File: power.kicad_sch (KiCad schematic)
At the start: 11 parts, among them U3 TLV71333PDQN

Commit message: schematic: more improvements towards R3
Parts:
- C14, C16: value 0.1uF -> 0u1
- R6: value 1.5K -> 1K5
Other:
- company: (none) -> Kalyan S, Vincent W, Kai G

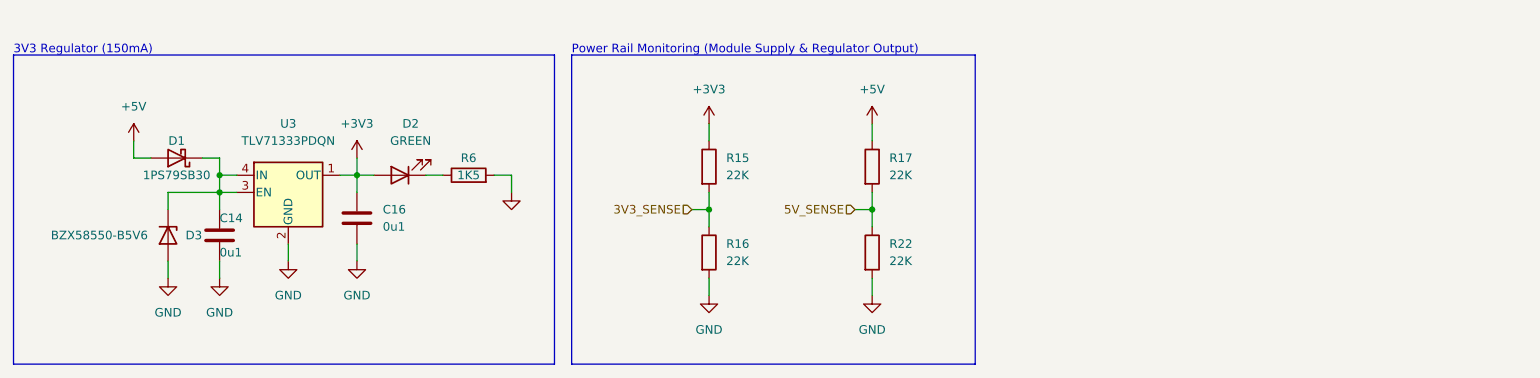
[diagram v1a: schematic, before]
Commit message: schematic: refresh sensors, mcu and redo pinout
    * update rp2040 -> rp2350b
    * update icm-42688p -> icm-45686
    * update bmm150 -> bmm350
    * add current sensing logic
    * change pinout count and update pinout
    * drop led and heater support
    * add can termination
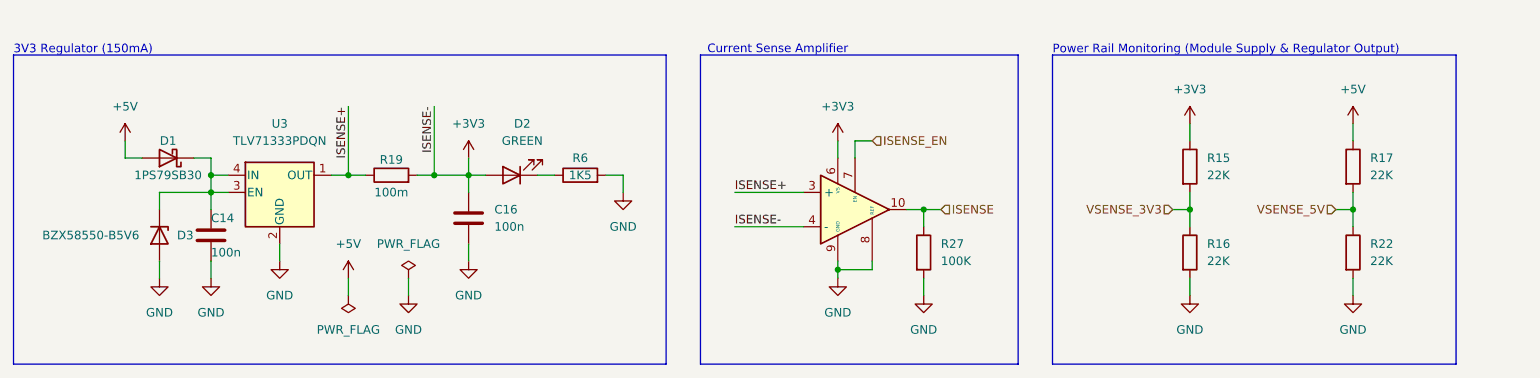
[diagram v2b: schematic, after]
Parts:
- added R19: 100m, symbol Device:R
- added R27: 100K, symbol Device:R
- added U9: ~, symbol Amplifier_Current_Extra:INA190
- C14, C16: value 0u1 -> 100n
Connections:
- net +3V3: now also R19.2, U9.4 (NC), U9.6 (VS); no longer U3.1 (OUT)
- net GND: now also R27.2, U9.8 (REF), U9.9 (GND)
- net 3V3_SENSE renamed VSENSE_3V3
- net 5V_SENSE renamed VSENSE_5V
- new net ISENSE: R27.1, U9.10
- new net ISENSE+: R19.1, U3.1 (OUT), U9.3 (+)
- new net ISENSE_EN: U9.7 (EN)
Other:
- note added: "Current Sense Amplifier"
- moved on the sheet: C14, C16, D1, D2, D3, R15, R16, R17, R22, R6, U3

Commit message: schematic: cleanup
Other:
- moved on the sheet: C14, C16, D1, D2, D3, R15, R16, R17, R19, R22, R27, R6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

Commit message: schematic: footprint assignment
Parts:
- R19: footprint (none) -> Resistor_SMD:R_0603_1608Metric
- R27: footprint (none) -> Resistor_SMD:R_0201_0603Metric
- U9: footprint (none) -> Package_DFN_QFN:Texas_RSW0010A_UQFN-10_1.4x1.8mm_P0.4mm
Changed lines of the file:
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@@
 			)
 		)
-		(property "Footprint" ""
+		(property "Footprint" "Package_DFN_QFN:Texas_RSW0010A_UQFN-10_1.4x1.8mm_P0.4mm"
 			(at 139.7 43.18 0)
 			(effects
@@
 		(pin "7"
 		)
-		(pin "4"
-		)
 		(pin "6"
 		)
@@
 			)
 		)
-		(property "Footprint" ""
+		(property "Footprint" "Resistor_SMD:R_0201_0603Metric"
 			(at 149.352 49.53 90)
 			(effects
@@
 			)
 		)
-		(property "Footprint" ""
+		(property "Footprint" "Resistor_SMD:R_0603_1608Metric"
 			(at 72.39 39.878 90)
 			(effects
